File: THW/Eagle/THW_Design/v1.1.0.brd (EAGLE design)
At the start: 50.6 x 182.7 mm, 34 parts, among them U1 ADA4091-2ARZ-RL

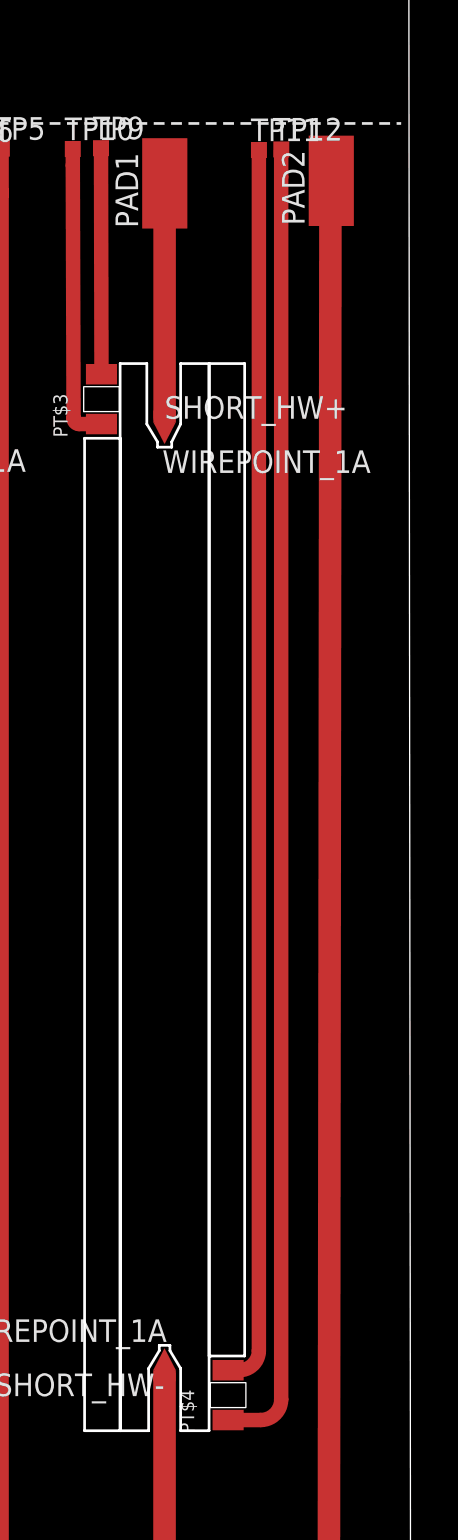
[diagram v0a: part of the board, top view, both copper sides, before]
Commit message: resistance on traces
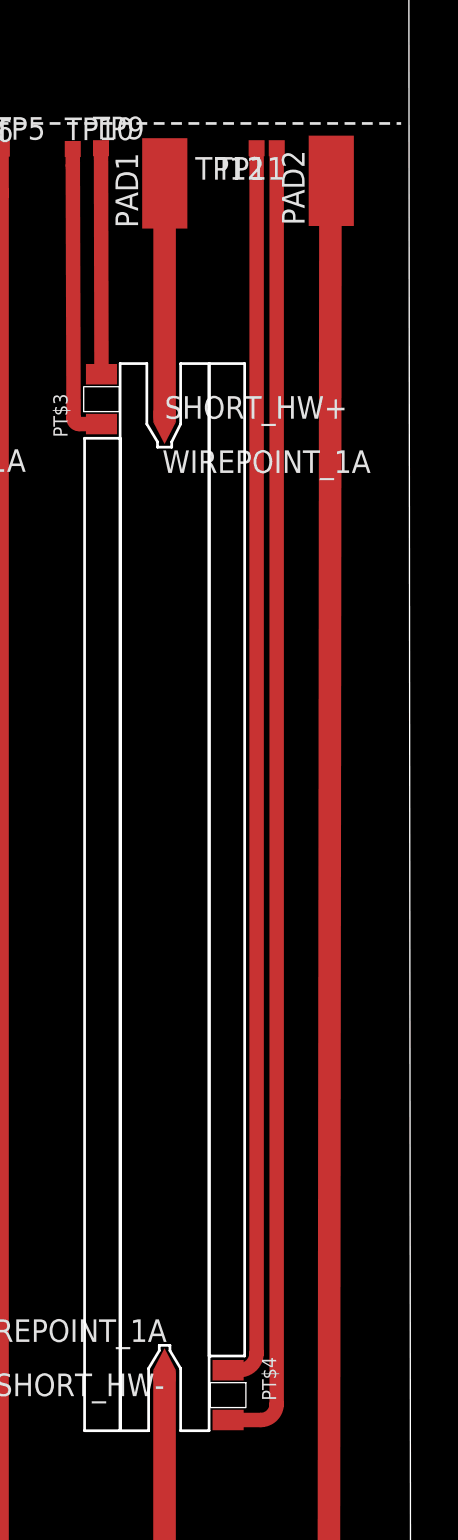
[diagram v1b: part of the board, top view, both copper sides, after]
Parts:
- moved TP12 1.39 mm to (41.9, 129.6), turned to 180 degrees
- moved TP11 1.01 mm to (43.0, 129.6), turned to 180 degrees
- turned PT$4 to 270 degrees
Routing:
- net T_S4+: track 69.7 -> 73.7 mm
- net T_S4-: track 73.8 -> 69.7 mm
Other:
- board text added: "R = 0.00498"
- board text added: "R = 0.00502"
- board text added: "R = 0.00760"
- board text added: "R = 0.00784"
- board text added: "R = 0.0101"
- board text added: "R = 0.0103"
- board text added: "R = 0.0418"
- board text added: "R = 0.0441"
- board text added: "R = 0.0535"
- board text added: "R = 0.0542"
- board text added: "R = 0.0735"
- board text added: "R = 0.0763"
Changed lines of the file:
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@@
 <setting verticaltext="up"/>
 </settings>
-<grid distance="1" unitdist="mm" unit="mm" style="lines" multiple="1" display="yes" altdistance="5" altunitdist="mil" altunit="mm"/>
+<grid distance="0.01" unitdist="mm" unit="mm" style="lines" multiple="1" display="yes" altdistance="5" altunitdist="mil" altunit="mm"/>
 <layers>
 <layer number="1" name="Top" color="4" fill="1" visible="yes" active="yes"/>
@@
 <wire x1="0" y1="131" x2="50" y2="131" width="0.1524" layer="21" style="longdash"/>
 <text x="0.127" y="131.191" size="0.4064" layer="21">CUT HERE</text>
+<text x="8" y="131" size="1.27" layer="48" rot="R90">R = 0.0542</text>
+<text x="17.399" y="131.064" size="1.27" layer="48" rot="R90">R = 0.00498</text>
+<text x="36.449" y="131.064" size="1.27" layer="48" rot="R90">R = 0.00502</text>
+<text x="46" y="131" size="1.27" layer="48" rot="R90">R = 0.0535</text>
+<text x="26" y="131" size="1.27" layer="48" rot="R90">R = 0.0735</text>
+<text x="28.081" y="131.064" size="1.27" layer="48" rot="R90">R = 0.0763</text>
+<text x="11.43" y="131.064" size="1.27" layer="48" rot="R90">R = 0.0103</text>
+<text x="13.208" y="131.064" size="1.27" layer="48" rot="R90">R = 0.00784</text>
+<text x="31.877" y="131.064" size="1.27" layer="48" rot="R90">R = 0.0101</text>
+<text x="33.528" y="131.064" size="1.27" layer="48" rot="R90">R = 0.00760</text>
+<text x="41.92" y="130.94" size="1.27" layer="48" rot="R90">R = 0.0418</text>
+<text x="43.58" y="131.04" size="1.27" layer="48" rot="R90">R = 0.0441</text>
 </plain>
 <attributes>
@@
 <attribute name="TP_SIGNAL_NAME" value="" x="31.537" y="129.564" size="1.778" layer="27" display="off"/>
 </element>
-<element name="TP11" library="testpad" library_urn="urn:adsk.eagle:library:385" package="TP09SQ" package3d_urn="urn:adsk.eagle:package:27957/1" value="TPSQTP09SQ" x="42.004" y="129.507">
-<attribute name="TP_SIGNAL_NAME" value="" x="42.004" y="129.507" size="1.778" layer="27" display="off"/>
-</element>
-<element name="TP12" library="testpad" library_urn="urn:adsk.eagle:library:385" package="TP09SQ" package3d_urn="urn:adsk.eagle:package:27957/1" value="TPSQTP09SQ" x="43.26" y="129.54">
-<attribute name="TP_SIGNAL_NAME" value="" x="43.26" y="129.54" size="1.778" layer="27" display="off"/>
+<element name="TP11" library="testpad" library_urn="urn:adsk.eagle:library:385" package="TP09SQ" package3d_urn="urn:adsk.eagle:package:27957/1" value="TPSQTP09SQ" x="43.004" y="129.61" rot="R180">
+<attribute name="TP_SIGNAL_NAME" value="" x="43.004" y="129.61" size="1.778" layer="27" rot="R180" display="off"/>
+</element>
+<element name="TP12" library="testpad" library_urn="urn:adsk.eagle:library:385" package="TP09SQ" package3d_urn="urn:adsk.eagle:package:27957/1" value="TPSQTP09SQ" x="41.873" y="129.61" rot="R180">
+<attribute name="TP_SIGNAL_NAME" value="" x="41.873" y="129.61" size="1.778" layer="27" rot="R180" display="off"/>
 </element>
 <element name="TP5" library="testpad" library_urn="urn:adsk.eagle:library:385" package="TP09SQ" package3d_urn="urn:adsk.eagle:package:27957/1" value="TPSQTP09SQ" x="27.551" y="129.587">
@@
 <element name="PT$2" library="PTS1206" package="CAPMP3216X166" value="PTS1206A" x="13.75" y="115.6" rot="R90"/>
 <element name="PT$3" library="PTS1206" package="CAPMP3216X166" value="PTS1206A" x="33.15" y="115.5" rot="R90"/>
-<element name="PT$4" library="PTS1206" package="CAPMP3216X166" value="PTS1206A" x="40.27" y="59.501" rot="R90"/>
+<element name="PT$4" library="PTS1206" package="CAPMP3216X166" value="PTS1206A" x="40.27" y="59.501" rot="R270"/>
 <element name="WP1" library="WIREPOINT" package="WIREPOINT" value="WIREPOINT_1A" x="14.141" y="12.433" rot="R180"/>
 <element name="U1" library="ADA4091-2ARZ-RL" package="SOIC127P600X175-8N" value="ADA4091-2ARZ-RL" x="46" y="160">
@@
 <wire x1="33.46" y1="162.23" x2="41" y2="160.0856" width="0" layer="19" extent="1-1"/>
 <wire x1="32.18" y1="155.26" x2="33.46" y2="162.23" width="0" layer="19" extent="1-1"/>
-<wire x1="34.26" y1="176.21" x2="48.27" y2="172" width="0" layer="19" extent="1-1"/>
+<wire x1="34.26" y1="176.21" x2="33.46" y2="162.23" width="0" layer="19" extent="1-1"/>
 <wire x1="6.32" y1="178.75" x2="34.26" y2="176.21" width="0" layer="19" extent="1-1"/>
 </signal>
@@
 <wire x1="43.5362" y1="160.635" x2="36.8" y2="176.21" width="0" layer="19" extent="1-1"/>
 <wire x1="19.94" y1="155.06" x2="43.5362" y2="160.635" width="0" layer="19" extent="1-1"/>
+<wire x1="3.78" y1="176.21" x2="19.94" y2="155.06" width="0" layer="19" extent="1-1"/>
 <wire x1="17.324" y1="127.605" x2="19.94" y2="155.06" width="0" layer="19" extent="1-1"/>
-<wire x1="3.78" y1="176.21" x2="31.72" y2="178.75" width="0" layer="19" extent="1-1"/>
 </signal>
 <signal name="VSS">
@@
 <contactref element="C2" pad="1"/>
 <wire x1="46.0856" y1="169" x2="45.73" y2="172" width="0" layer="19" extent="1-1"/>
-<wire x1="39.34" y1="176.21" x2="46.0856" y2="169" width="0" layer="19" extent="1-1"/>
 <wire x1="48.4638" y1="161.905" x2="46.0856" y2="169" width="0" layer="19" extent="1-1"/>
 <wire x1="41" y1="161.9144" x2="48.4638" y2="161.905" width="0" layer="19" extent="1-1"/>
+<wire x1="39.34" y1="176.21" x2="45.73" y2="172" width="0" layer="19" extent="1-1"/>
 <wire x1="12.29" y1="168.4" x2="39.34" y2="176.21" width="0" layer="19" extent="1-1"/>
 </signal>
@@
 <contactref element="JP1" pad="7"/>
 <contactref element="PT$4" pad="+"/>
-<wire x1="40.27" y1="60.901" x2="40.901" y2="60.901" width="0.8128" layer="1"/>
-<wire x1="40.901" y1="60.901" x2="42" y2="62" width="0.8128" layer="1" curve="90"/>
-<wire x1="42" y1="129.503" x2="42.004" y2="129.507" width="0.8128" layer="1" curve="-90"/>
-<wire x1="42" y1="62" x2="42" y2="129.503" width="0.8128" layer="1"/>
-<wire x1="42.004" y1="129.507" x2="19.72" y2="143.63" width="0" layer="19" extent="1-1"/>
+<wire x1="40.27" y1="58.101" x2="42.101" y2="58.101" width="0.8128" layer="1"/>
+<wire x1="42.101" y1="58.101" x2="43" y2="59" width="0.8128" layer="1" curve="90"/>
+<wire x1="43" y1="129.606" x2="43.004" y2="129.61" width="0.8128" layer="1" curve="-90"/>
+<wire x1="43" y1="59" x2="43" y2="129.606" width="0.8128" layer="1"/>
+<wire x1="43.004" y1="129.61" x2="19.72" y2="143.63" width="0" layer="19" extent="1-1"/>
 </signal>
 <signal name="T_S4-">
@@
 <contactref element="JP1" pad="8"/>
 <contactref element="PT$4" pad="-"/>
-<wire x1="40.27" y1="58.101" x2="42.101" y2="58.101" width="0.8128" layer="1"/>
-<wire x1="42.101" y1="58.101" x2="43.254" y2="59.254" width="0.8128" layer="1" curve="90"/>
-<wire x1="43.254" y1="59.254" x2="43.254" y2="128" width="0.8128" layer="1"/>
-<wire x1="43.254" y1="128" x2="43.254" y2="129.534" width="0.8128" layer="1"/>
-<wire x1="43.254" y1="129.534" x2="43.26" y2="129.54" width="0.8128" layer="1" curve="-90"/>
-<wire x1="43.26" y1="129.54" x2="19.72" y2="146.17" width="0" layer="19" extent="1-1"/>
+<wire x1="40.27" y1="60.901" x2="40.901" y2="60.901" width="0.8128" layer="1"/>
+<wire x1="40.901" y1="60.901" x2="41.873" y2="61.873" width="0.8128" layer="1" curve="90"/>
+<wire x1="41.873" y1="61.873" x2="41.873" y2="129.61" width="0.8128" layer="1"/>
+<wire x1="41.873" y1="129.61" x2="19.72" y2="146.17" width="0" layer="19" extent="1-1"/>
 </signal>
 <signal name="N$2">

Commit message: new version
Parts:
- removed JP1: (no value), pinhead:2X10
- removed PAD1, PAD2, PAD4: (no value), wirepad:SMD2,54-5,08
- removed WP1: WIREPOINT_1A, WIREPOINT:WIREPOINT
- added JP3: (no value), pinhead:2X12
- added LONG_HW-: WIREPOINT_1A, WIREPOINT:WIREPOINT
- added PAD5, PAD6, PAD7: (no value), wirepad:SMD2,54-5,08
- added PT$5, PT$6: PTS1206A, PTS1206:CAPMP3216X166
- added TP1, TP13, TP14, TP15, TP16, TP17, TP18, TP19, TP2, TP20, TP21, TP22, TP23, TP24, TP25, TP26, TP27, TP28, TP3, TP4: TPTP10SQ, testpad:TP10SQ
- TP10, TP11, TP12, TP5, TP6, TP7, TP8, TP9: value TPSQTP09SQ -> TPTP10SQ; device testpad:TP09SQ -> testpad:TP10SQ
- moved PT$3 71.7 mm to (59.9, 49.0), turned to 270 degrees
- moved SHORT_HW- 54.7 mm to (43.7, 8.60), turned to 0 degrees
- moved TP8 53.9 mm to (64.4, 120.9)
- moved PT$4 53.8 mm to (36.6, 5.81), turned to 180 degrees
- moved PT$2 52.3 mm to (59.9, 91.0), turned to 270 degrees
- moved TP7 52.3 mm to (64.6, 123.1)
- moved TP6 42.1 mm to (67.0, 120.9)
- moved TP5 39.0 mm to (66.0, 123.0)
- moved TP12 36.5 mm to (6.31, 121.2), turned to 0 degrees
- moved TP11 36.3 mm to (7.29, 123.0), turned to 0 degrees
- moved TP9 25.4 mm to (8.61, 123.0)
- moved TP10 23.1 mm to (9.99, 121.2)
- moved PT$1 19.8 mm to (13.5, 28.0), turned to 90 degrees
- moved C1 10.0 mm to (49.0, 155.0)
- moved C2 10.0 mm to (55.0, 163.0)
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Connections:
- removed net T_S1+: JP1.1, PT$1.+, TP5.TP
- removed net T_S1-: JP1.2, PT$1.-, TP6.TP
- removed net T_S2+: JP1.3, PT$2.+, TP7.TP
- removed net T_S2-: JP1.4, PT$2.-, TP8.TP
- removed net T_S3+: JP1.5, PT$3.+, TP9.TP
- removed net T_S3-: JP1.6, PT$3.-, TP10.TP
- removed net T_S4+: JP1.7, PT$4.+, TP11.TP
- removed net T_S4-: JP1.8, PT$4.-, TP12.TP
- new net LONG_HW_SENS+: LONG_HW+.P$2, TP27.TP
- new net LONG_HW_SENS-: LONG_HW-.P$1, TP28.TP
- new net PT1_+: JP3.1, PT$2.+, TP1.TP
- new net PT1_-: JP3.2, PT$2.-, TP3.TP
- new net PT1_S+: JP3.3, PT$2.SENS+, TP2.TP
- new net PT1_S-: JP3.4, PT$2.SENS-, TP4.TP
- new net PT2_+: JP3.5, PT$3.+, TP5.TP
- new net PT2_-: JP3.6, PT$3.-, TP7.TP
- new net PT2_S+: JP3.7, PT$3.SENS+, TP6.TP
- new net PT2_S-: JP3.8, PT$3.SENS-, TP8.TP
- new net PT3_+: JP3.9, PT$1.+, TP9.TP
- new net PT3_-: JP3.10, PT$1.-, TP11.TP
- new net PT3_S+: JP3.11, PT$1.SENS+, TP10.TP
- new net PT3_S-: JP3.12, PT$1.SENS-, TP12.TP
- new net PT4_+: JP3.13, PT$4.+, TP13.TP
- new net PT4_-: JP3.14, PT$4.-, TP15.TP
- new net PT4_S+: JP3.15, PT$4.SENS+, TP14.TP
- new net PT4_S-: JP3.16, PT$4.SENS-, TP16.TP
- new net PT5_+: JP3.17, PT$5.+, TP17.TP
- new net PT5_-: JP3.18, PT$5.-, TP19.TP
- new net PT5_S+: JP3.19, PT$5.SENS+, TP18.TP
- new net PT5_S-: JP3.20, PT$5.SENS-, TP20.TP
- new net PT6_+: JP3.21, PT$6.+, TP21.TP
- new net PT6_-: JP3.22, PT$6.-, TP23.TP
- new net PT6_S+: JP3.23, PT$6.SENS+, TP22.TP
- new net PT6_S-: JP3.24, PT$6.SENS-, TP24.TP
- new net SHORT_HW_SENS+: SHORT_HW+.P$2, TP26.TP
- new net SHORT_HW_SENS-: SHORT_HW-.P$1, TP25.TP
- net LONG_HW+: now also PAD7.1; no longer PAD4.1, SV1.1
- net LONG_HW-: now also LONG_HW-.P$2; no longer SV1.2, WP1.P$1
- net SHORT_HW+: now also PAD5.1; no longer PAD1.1, SV1.35
- net SHORT_HW-: now also PAD6.1, SHORT_HW-.P$2; no longer PAD2.1, SHORT_HW-.P$1, SV1.36
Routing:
- net PT4_+: track 0.00 -> 151.2 mm, vias 0 -> 1
- net PT4_-: track 0.00 -> 151.1 mm, vias 0 -> 1
- net PT4_S+: track 0.00 -> 149.6 mm, vias 0 -> 1
- net PT4_S-: track 0.00 -> 148.4 mm, vias 0 -> 1
- net LONG_HW_SENS-: track 0.00 -> 142.5 mm, vias 0 -> 1
- net SHORT_HW_SENS-: track 0.00 -> 141.4 mm, vias 0 -> 1
- net T_S1+: track 127.4 -> 0.00 mm
- net T_S1-: track 122.9 -> 0.00 mm
- net PT3_S-: track 0.00 -> 100.8 mm, vias 0 -> 1
- net PT3_-: track 0.00 -> 97.6 mm, vias 0 -> 1
- net PT3_+: track 0.00 -> 93.8 mm, vias 0 -> 1
- net PT3_S+: track 0.00 -> 92.7 mm, vias 0 -> 1
- net PT2_S+: track 0.00 -> 81.0 mm, vias 0 -> 1
- net PT2_+: track 0.00 -> 76.2 mm, vias 0 -> 1
- net T_S4+: track 73.7 -> 0.00 mm
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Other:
- board size 50.6 x 182.7 mm -> 73.5 x 175.6 mm
- board text removed: "CUT HERE"
- board text removed: "R = 0.00498"
- board text removed: "R = 0.00502"
- board text removed: "R = 0.00760"
- board text removed: "R = 0.00784"
- board text removed: "R = 0.0101"
- board text removed: "R = 0.0103"
- board text removed: "R = 0.0418"
- board text removed: "R = 0.0441"
- board text removed: "R = 0.0535"
- board text removed: "R = 0.0542"
- board text removed: "R = 0.0735"
- board text removed: "R = 0.0763"

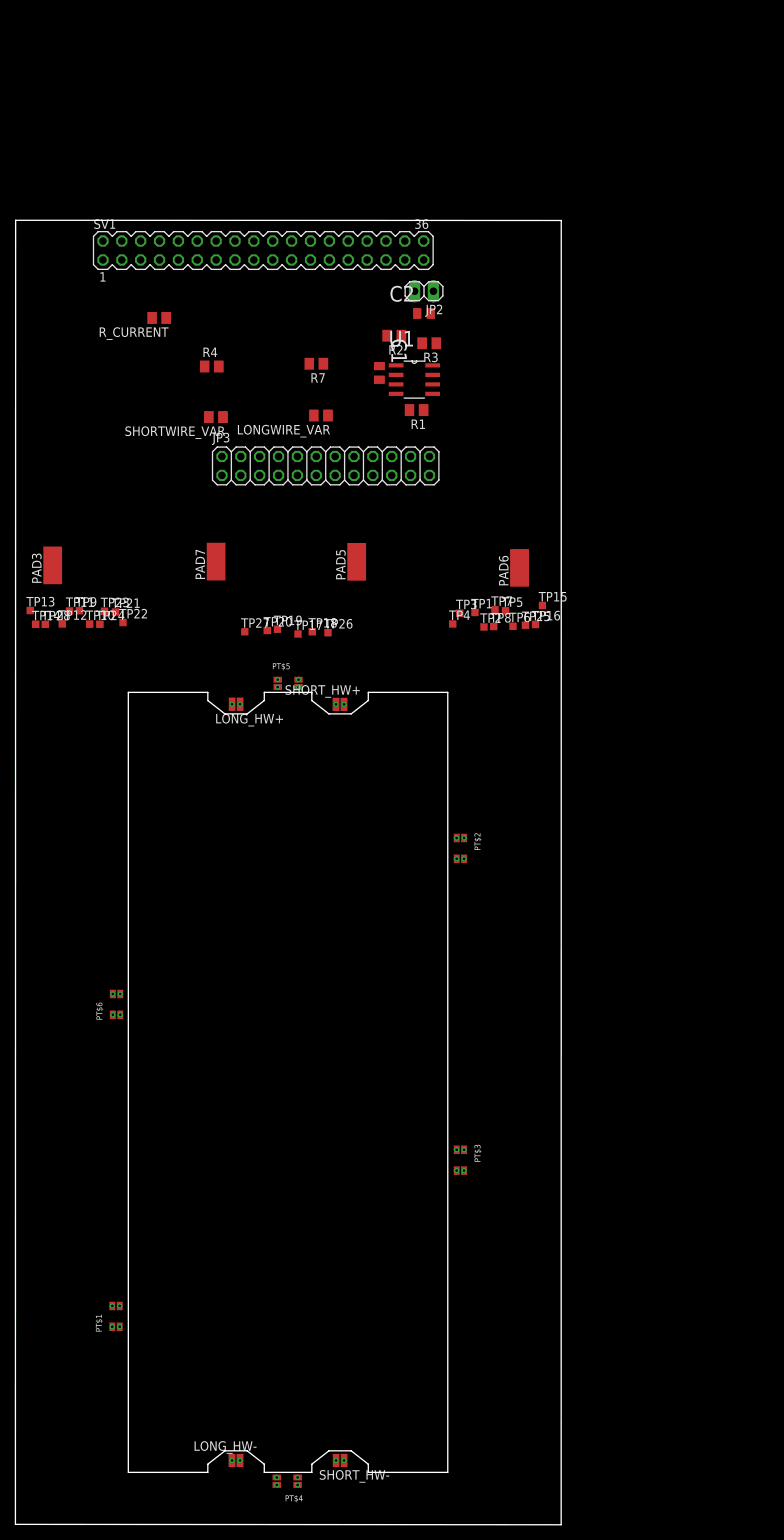
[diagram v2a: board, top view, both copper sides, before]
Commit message: adding one current source to PT sensors
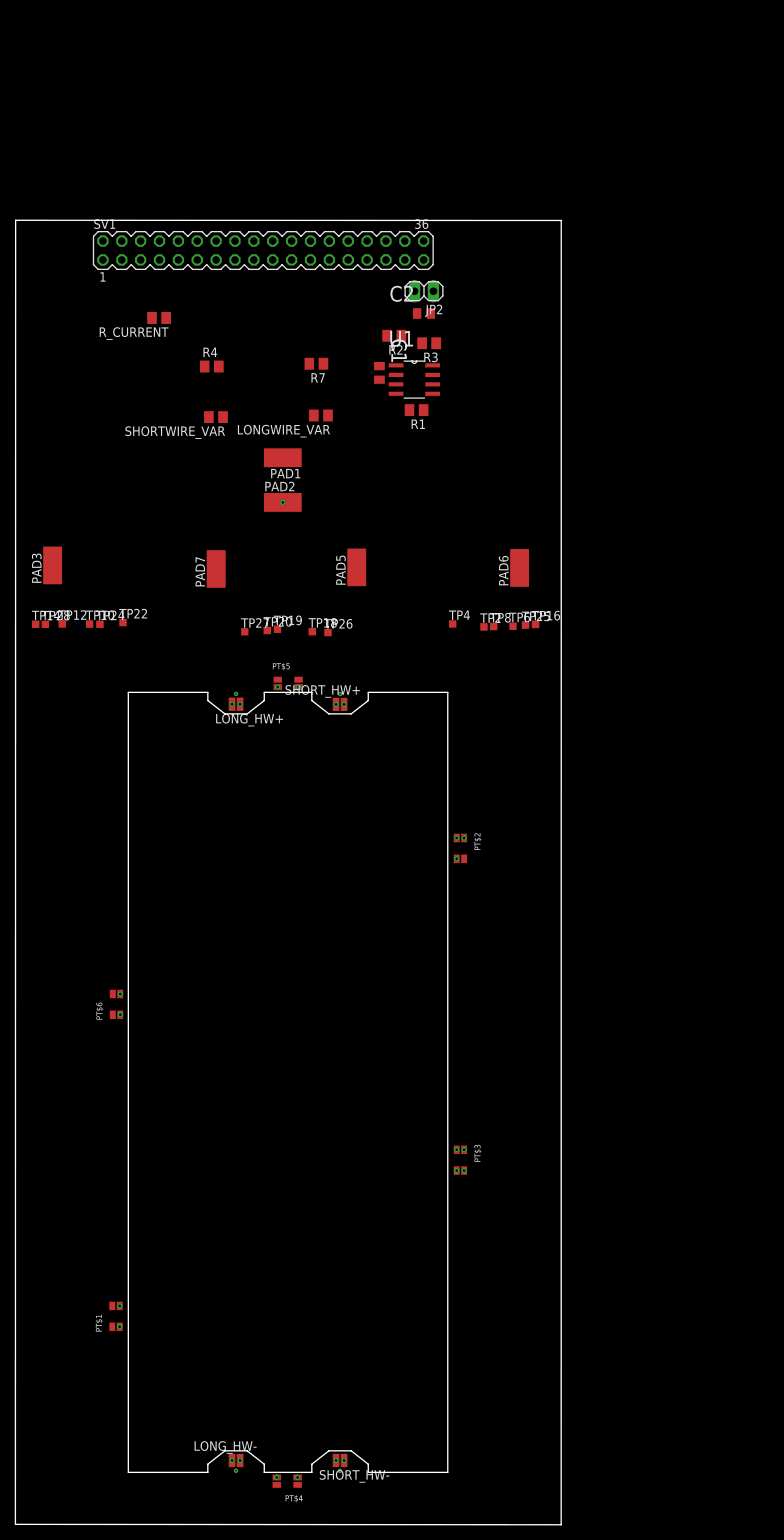
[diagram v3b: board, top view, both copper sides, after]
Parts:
- removed JP3: (no value), pinhead:2X12
- removed TP1, TP11, TP13, TP15, TP17, TP21, TP23, TP3, TP5, TP7, TP9: TPTP10SQ, testpad:TP10SQ
- added PAD1, PAD2: (no value), wirepad:SMD2,54-5,08
- moved PAD7 1.00 mm to (27.0, 128.6)
- moved PAD5 0.74 mm to (46.0, 128.8)
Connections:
- removed net PT1_+: JP3.1, PT$2.+, TP1.TP
- removed net PT1_-: JP3.2, PT$2.-, TP3.TP
- removed net PT2_+: JP3.5, PT$3.+, TP5.TP
- removed net PT2_-: JP3.6, PT$3.-, TP7.TP
- removed net PT3_+: JP3.9, PT$1.+, TP9.TP
- removed net PT3_-: JP3.10, PT$1.-, TP11.TP
- removed net PT4_+: JP3.13, PT$4.+, TP13.TP
- removed net PT4_-: JP3.14, PT$4.-, TP15.TP
- removed net PT5_+: JP3.17, PT$5.+, TP17.TP
- removed net PT5_-: JP3.18, PT$5.-, TP19.TP
- removed net PT6_+: JP3.21, PT$6.+, TP21.TP
- removed net PT6_-: JP3.22, PT$6.-, TP23.TP
- new net B$2: PT$1.-
- new net PT+: PAD1.1, PT$1.+, PT$2.+, PT$3.+, PT$4.+, PT$5.+, PT$6.+
- new net PT-: PAD2.1, PT$2.-, PT$3.-, PT$4.-, PT$5.-, PT$6.-
- net PT1_S+: no longer JP3.3
- net PT1_S-: no longer JP3.4
- net PT2_S+: no longer JP3.7
- net PT2_S-: no longer JP3.8
- net PT3_S+: no longer JP3.11
- net PT3_S-: no longer JP3.12
- net PT4_S+: no longer JP3.15
- net PT4_S-: no longer JP3.16
- net PT5_S+: no longer JP3.19
- net PT5_S-: no longer JP3.20
- net PT6_S+: no longer JP3.23
- net PT6_S-: no longer JP3.24
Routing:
- net PT4_+: track 151.2 -> 0.00 mm, vias 1 -> 0
- net PT4_-: track 151.1 -> 0.00 mm, vias 1 -> 0
- net PT-: track 0.00 -> 149.4 mm, vias 0 -> 3
- net PT3_-: track 97.6 -> 0.00 mm, vias 1 -> 0
- net PT3_+: track 93.8 -> 0.00 mm, vias 1 -> 0
- net PT2_+: track 76.2 -> 0.00 mm, vias 1 -> 0
- net PT2_-: track 72.3 -> 0.00 mm, vias 1 -> 0
- net PT6_-: track 51.6 -> 0.00 mm, vias 1 -> 0
- net PT6_+: track 47.6 -> 0.00 mm, vias 1 -> 0
- net PT1_+: track 30.5 -> 0.00 mm, vias 1 -> 0
- net PT1_-: track 26.5 -> 0.00 mm, vias 1 -> 0
- net PT+: track 0.00 -> 6.17 mm, vias 0 -> 1
- net PT5_+: track 5.17 -> 0.00 mm, vias 1 -> 0
- net PT5_-: track 5.14 -> 0.00 mm, vias 1 -> 0
